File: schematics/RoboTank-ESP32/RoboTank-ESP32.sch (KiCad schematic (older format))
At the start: 42 parts, among them M1 Arm Servo 0, M2 Arm Servo 1, M3 Arm Servo 2, M4 Arm Servo 3, M5 Arm Servo 4, M6 Arm Servo 5, M7 Chassis Motor 1, M8 Ultrasonic Sensor Servo, M9 Chassis Motor 2, SW1 Main Switch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

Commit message: More work on schematics
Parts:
- added D11: LED, symbol Device:LED
- added R1: 1k, symbol Device:R
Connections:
- net GND: now also R1.2
- net +3V3: now reaches U10.1 (VCC), U11.1 (VCC), U12.1 (VCC), U13.1 (VCCA), U15.16 (VDD), U5.3 (VCCA), U8.2 (3V3), U9.1 (VCC)
- net +5V: now reaches C1.1, D10.1 (VDD), D5.1 (VDD), D6.1 (VDD), D7.1 (VDD), D8.1 (VDD), D9.1 (VDD), U13.14 (VCCB), U14.6 (V+), U6.7 (5V), U7.1 (VCC), U8.20 (5V)
- net at U8.6 (IO34): now also U11.3 (OUT); no longer U5.5 (A1)
- net at U8.7 (IO35): now also U12.3 (OUT); no longer U5.4 (A2)
- net at U8.8 (IO32): now also U5.5 (A1); no longer U11.3 (OUT)
- net at U8.9 (IO33): now also U5.4 (A2); no longer U12.3 (OUT)
- net +5VP: now reaches M1.2 (+), M2.2 (+), M3.2 (+), M4.2 (+), M5.2 (+), M6.2 (+), M8.2 (+), U1.4 (OUT+), U4.5 (VCC), U4.6 (V+), U5.7 (VCCB)
- net at D5.2 (DOUT): now also D7.4 (DIN)
- net at U15.15 (P06): now also D11.1 (K)
- net at D7.2 (DOUT): now also D9.4 (DIN)
- net at D6.2 (DOUT): now also D8.4 (DIN)
- net at D8.2 (DOUT): now also D10.4 (DIN)
- new net: D11.2 (A), R1.1
- no-connect marks 0 -> 41
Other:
- note added: "5V YELLOW"
- note added: "Arm Power Supply (YELLOW)"
- note added: "Main Power Supply (RED)"
- note removed: "5V"
- note removed: "Arm Power Supply"
- note removed: "Main Power Supply"
- moved on the sheet: M3, M4, M5, M6, M8, U15

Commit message: Schematics finalized
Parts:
- removed U5: TXB0102DCT, Package_SO:TSSOP-8_3x3mm_P0.65mm, symbol Logic_LevelTranslator:TXB0102DCT
- added U5: TXB0104PW, Package_SO:TSSOP-14_4.4x5mm_P0.65mm, symbol Logic_LevelTranslator:TXB0104PW
- added U7: FS-iA6B, symbol !mrach_custom:FS-iA6B
- renumbered M9 to M8, M8 to M9, U7 to U14, U14 to U15, U15 to U16
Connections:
- net +3V3: now also U5.14 (VCCB)
- net +5VP: now also U5.1 (VCCA), U7.15 (V+(7x))
- net GND: now also U5.7 (GND), U7.10 (GND(7x))
- net at U4.3 (SCL): now also U5.3 (A2)
- net at U4.4 (SDA): now also U5.2 (A1)
- net at U13.2 (A1): now also U8.14 (IO12); no longer U8.35 (IO21)
- net at U13.3 (A2): now also U8.13 (IO14); no longer U8.33 (IO19)
- net at U13.4 (A3): now also U8.12 (IO27); no longer U8.32 (IO18)
- net at U13.5 (A4): now also U8.11 (IO26)
- net at U16.10 (P05): now also U8.6 (IO34); no longer U8.38 (IO22)
- net at U16.15 (P06): now also D11.2 (A); no longer D11.1 (K)
- net at U16.7 (P04): now also U8.7 (IO35); no longer U8.39 (IO23)
- net at U11.3 (OUT): now also U8.30 (IO17); no longer U8.6 (IO34)
- net at U9.3 (OUT): now also U8.32 (IO18); no longer U8.10 (IO25)
- net at U10.3 (OUT): now also U8.33 (IO19); no longer U8.11 (IO26)
- net at U12.3 (OUT): now also U8.31 (IO5); no longer U8.7 (IO35)
- net at U8.8 (IO32): now also U5.13 (B1)
- net at U8.9 (IO33): now also U5.12 (B2)
- net at R1.1: now also D11.1 (K); no longer D11.2 (A)
- new net: U5.11 (B3), U8.10 (IO25)
- new net: U5.4 (A3), U7.11 (S)
- no-connect marks 41 -> 52
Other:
- note added: "RC Receiver"
- moved on the sheet: C1, D1, D11, D2, D3, D4, M9, R1, U1, U13, U14, U4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

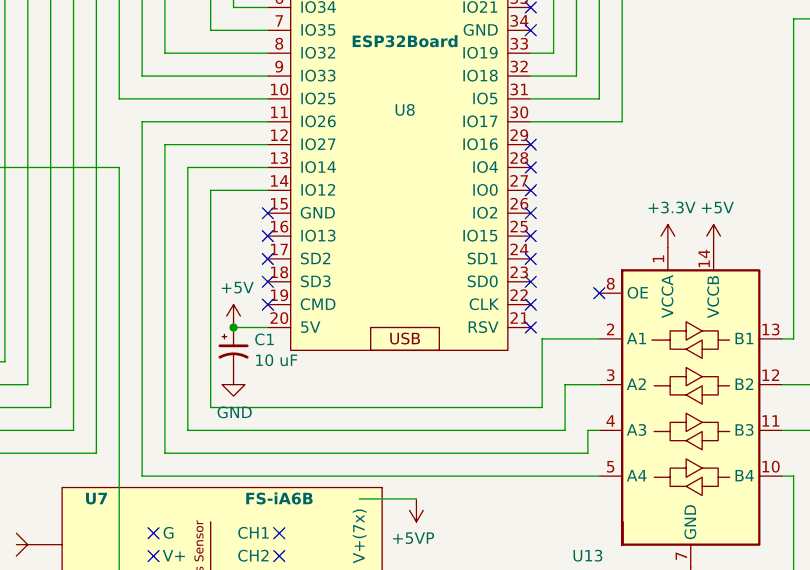
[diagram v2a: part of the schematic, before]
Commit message: Drafts: web Server OTA, sound module, RC module
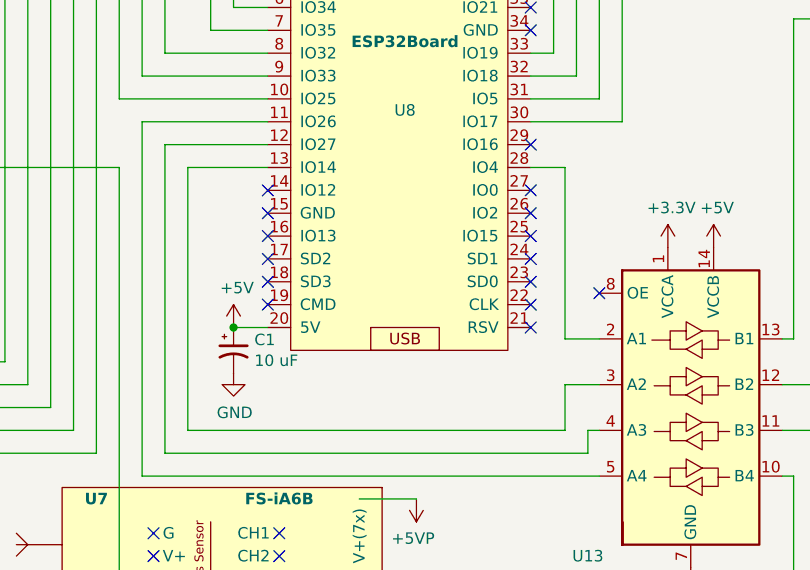
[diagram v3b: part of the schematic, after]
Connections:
- net at U13.2 (A1): now also U8.28 (IO4); no longer U8.14 (IO12)
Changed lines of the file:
@@
 NoConn ~ 7700 3500
 NoConn ~ 7700 4000
-NoConn ~ 7700 4100
 NoConn ~ 7700 4200
 NoConn ~ 7700 4300
@@
 	7850 5050 7850 5250
 Wire Wire Line
-	7750 4850 7750 5150
-Wire Wire Line
-	7750 4850 8000 4850
+	7850 4850 8000 4850
 Wire Wire Line
 	7850 5250 6200 5250
 Wire Wire Line
-	7750 5150 6300 5150
-Wire Wire Line
 	6200 4100 6550 4100
 Wire Wire Line
 	6200 4100 6200 5250
-Wire Wire Line
-	6300 4200 6300 5150
-Wire Wire Line
-	6300 4200 6550 4200
 Wire Wire Line
 	8950 5050 8950 4200
@@
 NoConn ~ 7700 3000
 NoConn ~ 7700 3100
+Wire Wire Line
+	7850 4850 7850 4100
+Wire Wire Line
+	7850 4100 7700 4100
+NoConn ~ 6550 4200
 $EndSCHEMATC

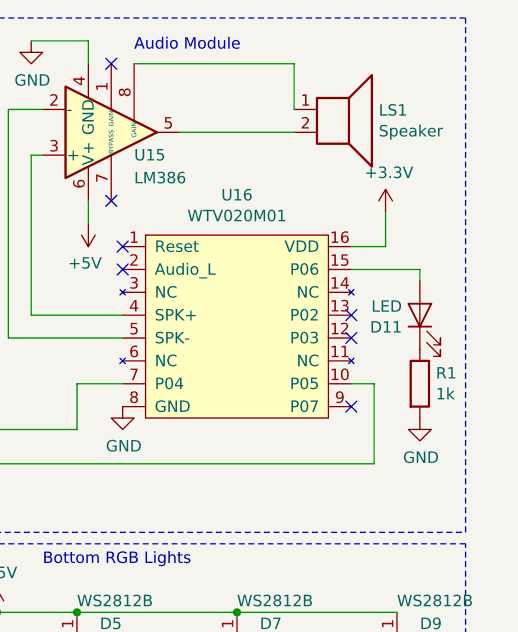
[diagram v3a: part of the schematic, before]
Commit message: Fixed bugs in WiFi code and sound module schematics.
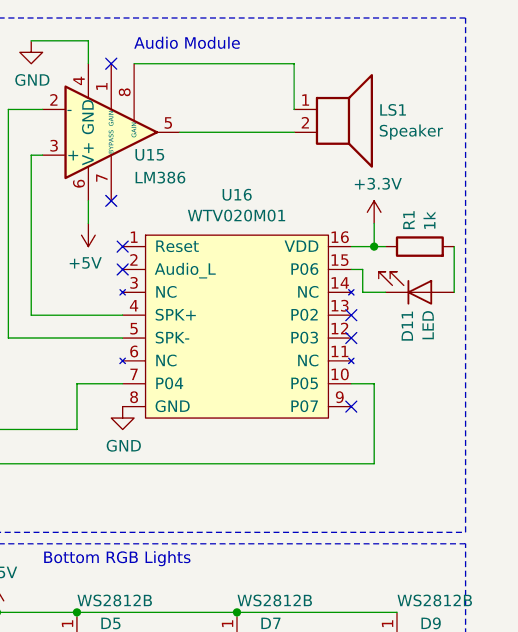
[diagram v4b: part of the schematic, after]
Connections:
- net +3V3: now also R1.1
- net GND: no longer R1.2
- net at U16.15 (P06): now also D11.1 (K); no longer D11.2 (A)
- new net: D11.2 (A), R1.2
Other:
- moved on the sheet: D11, R1
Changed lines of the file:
@@
 L power:+3.3V #PWR050
 U 1 1 5D9D01E0
-P 10800 1400
-F 0 "#PWR050" H 10800 1250 50  0001 C CNN
-F 1 "+3.3V" H 10815 1573 50  0000 C CNN
-F 2 "" H 10800 1400 50  0001 C CNN
-F 3 "" H 10800 1400 50  0001 C CNN
-	1    10800 1400
-	1    0    0    -1
-$EndComp
-Wire Wire Line
-	10650 1550 10800 1550
+P 10750 1450
+F 0 "#PWR050" H 10750 1300 50  0001 C CNN
+F 1 "+3.3V" H 10765 1623 50  0000 C CNN
+F 2 "" H 10750 1450 50  0001 C CNN
+F 3 "" H 10750 1450 50  0001 C CNN
+	1    10750 1450
+	1    0    0    -1
+$EndComp
+Wire Wire Line
+	10650 1550 10750 1550
 $Comp
 L power:+3.3V #PWR038
@@
 	5850 7500 5850 7600
 Wire Wire Line
-	10800 1550 10800 1400
-Wire Wire Line
-	10650 1650 10950 1650
-Wire Wire Line
-	10950 1650 10950 1700
-$Comp
-L power:GND #PWR051
-U 1 1 5DF1097D
-P 10950 2300
-F 0 "#PWR051" H 10950 2050 50  0001 C CNN
-F 1 "GND" H 10955 2127 50  0000 C CNN
-F 2 "" H 10950 2300 50  0001 C CNN
-F 3 "" H 10950 2300 50  0001 C CNN
-	1    10950 2300
-	1    0    0    -1
-$EndComp
+	10650 1650 10700 1650
+Wire Wire Line
+	10700 1650 10700 1750
 $Comp
 L Device:R R1
 U 1 1 5DEEC76B
-P 10950 2150
-F 0 "R1" H 11020 2196 50  0000 L CNN
-F 1 "1k" H 11020 2105 50  0000 L CNN
-F 2 "" V 10880 2150 50  0001 C CNN
-F 3 "~" H 10950 2150 50  0001 C CNN
-	1    10950 2150
-	1    0    0    -1
+P 10950 1550
+F 0 "R1" H 11020 1596 50  0000 L CNN
+F 1 "1k" H 11020 1505 50  0000 L CNN
+F 2 "" V 10880 1550 50  0001 C CNN
+F 3 "~" H 10950 1550 50  0001 C CNN
+	1    10950 1550
+	0    -1   -1   0
 $EndComp
 $Comp
 L Device:LED D11
 U 1 1 5DDF0B9E
-P 10950 1850
-F 0 "D11" V 10897 1928 50  0000 L CNN
-F 1 "LED" V 10988 1928 50  0000 L CNN
-F 2 "" H 10950 1850 50  0001 C CNN
-F 3 "~" H 10950 1850 50  0001 C CNN
-	1    10950 1850
-	0    -1   -1   0
+P 10950 1750
+F 0 "D11" V 10897 1828 50  0000 L CNN
+F 1 "LED" V 10988 1828 50  0000 L CNN
+F 2 "" H 10950 1750 50  0001 C CNN
+F 3 "~" H 10950 1750 50  0001 C CNN
+	1    10950 1750
+	1    0    0    1
 $EndComp
 NoConn ~ 6550 2900
@@
 	7850 4100 7700 4100
 NoConn ~ 6550 4200
+Wire Wire Line
+	10700 1750 10800 1750
+Wire Wire Line
+	11100 1550 11100 1750
+Wire Wire Line
+	10750 1450 10750 1550
+Connection ~ 10750 1550
+Wire Wire Line
+	10750 1550 10800 1550
 $EndSCHEMATC
